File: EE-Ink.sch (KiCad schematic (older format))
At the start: 32 parts

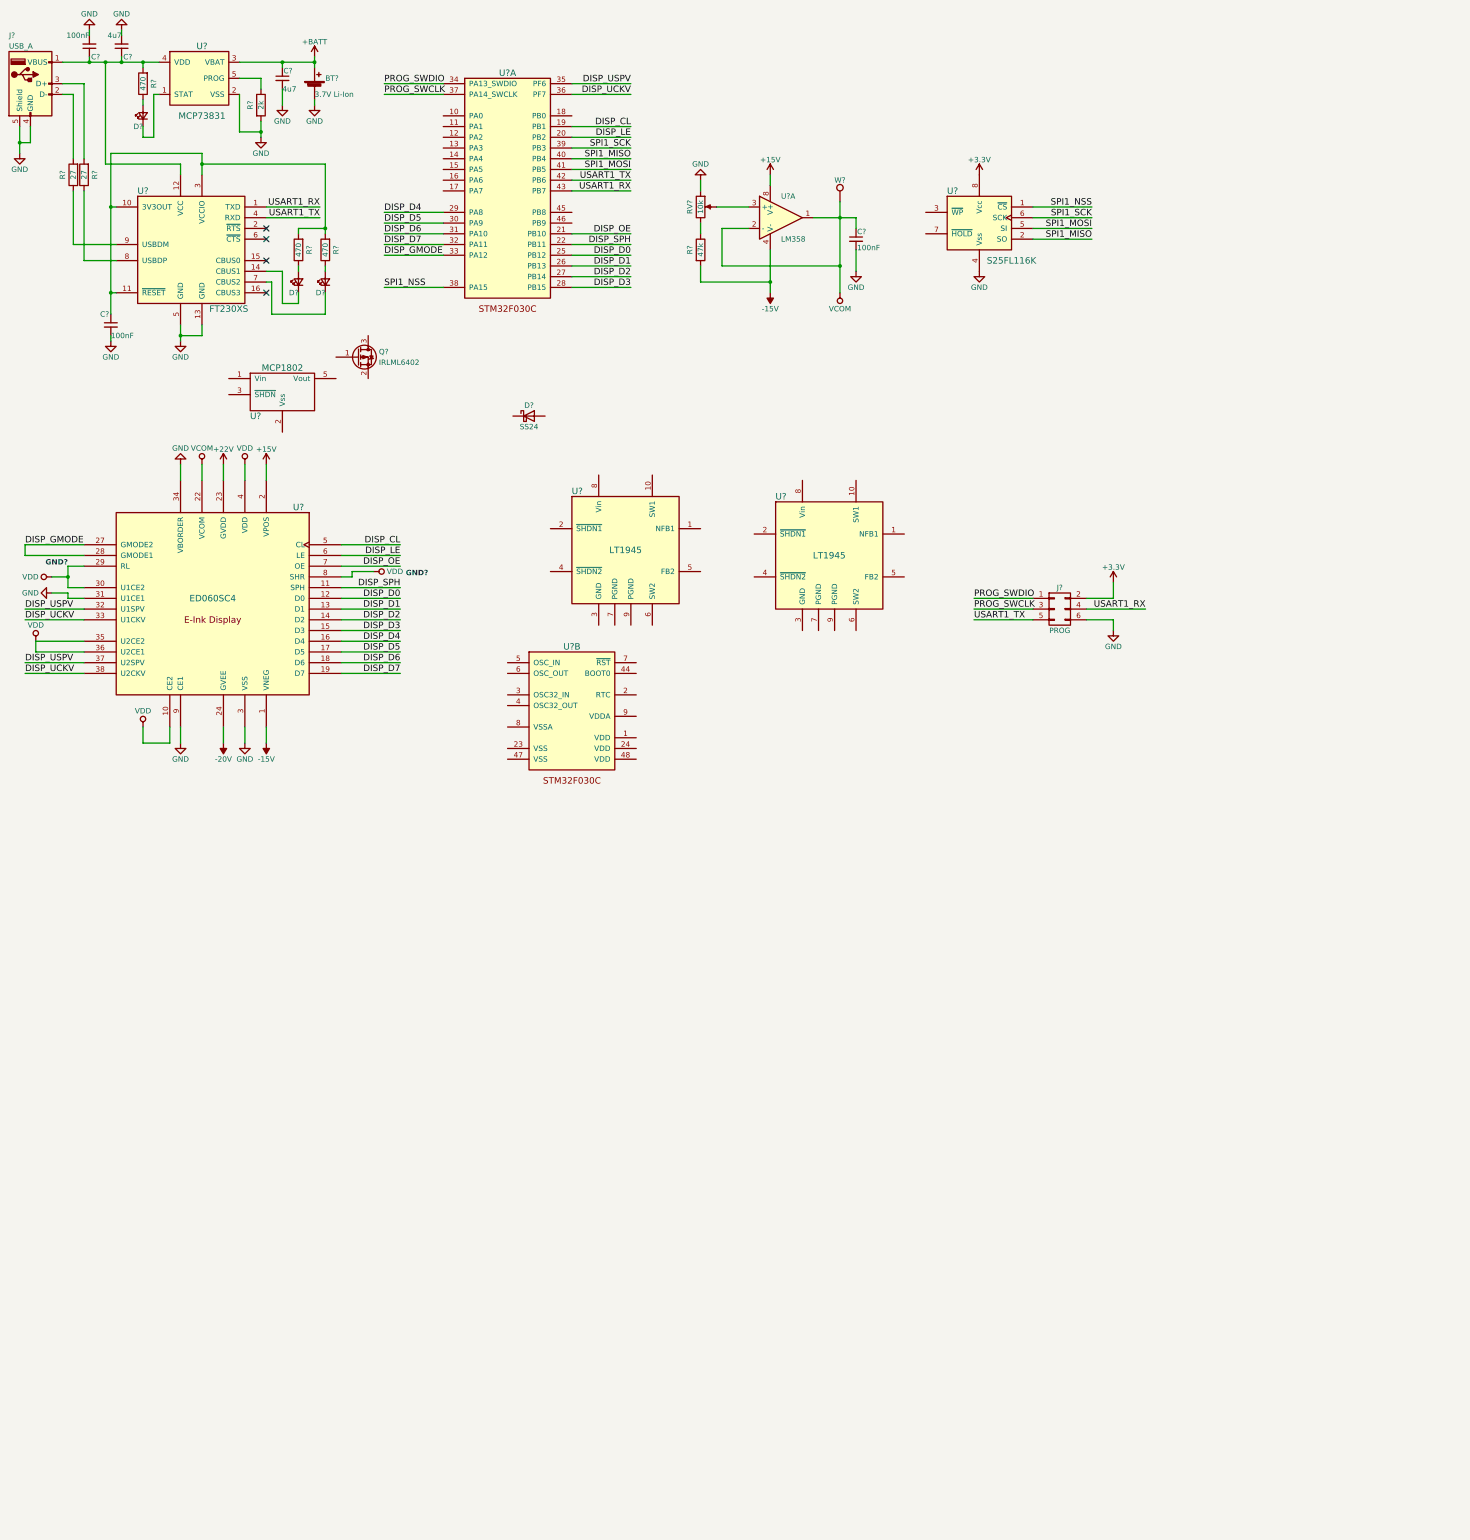
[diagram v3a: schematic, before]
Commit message: Wired up first boost circuit according to example.
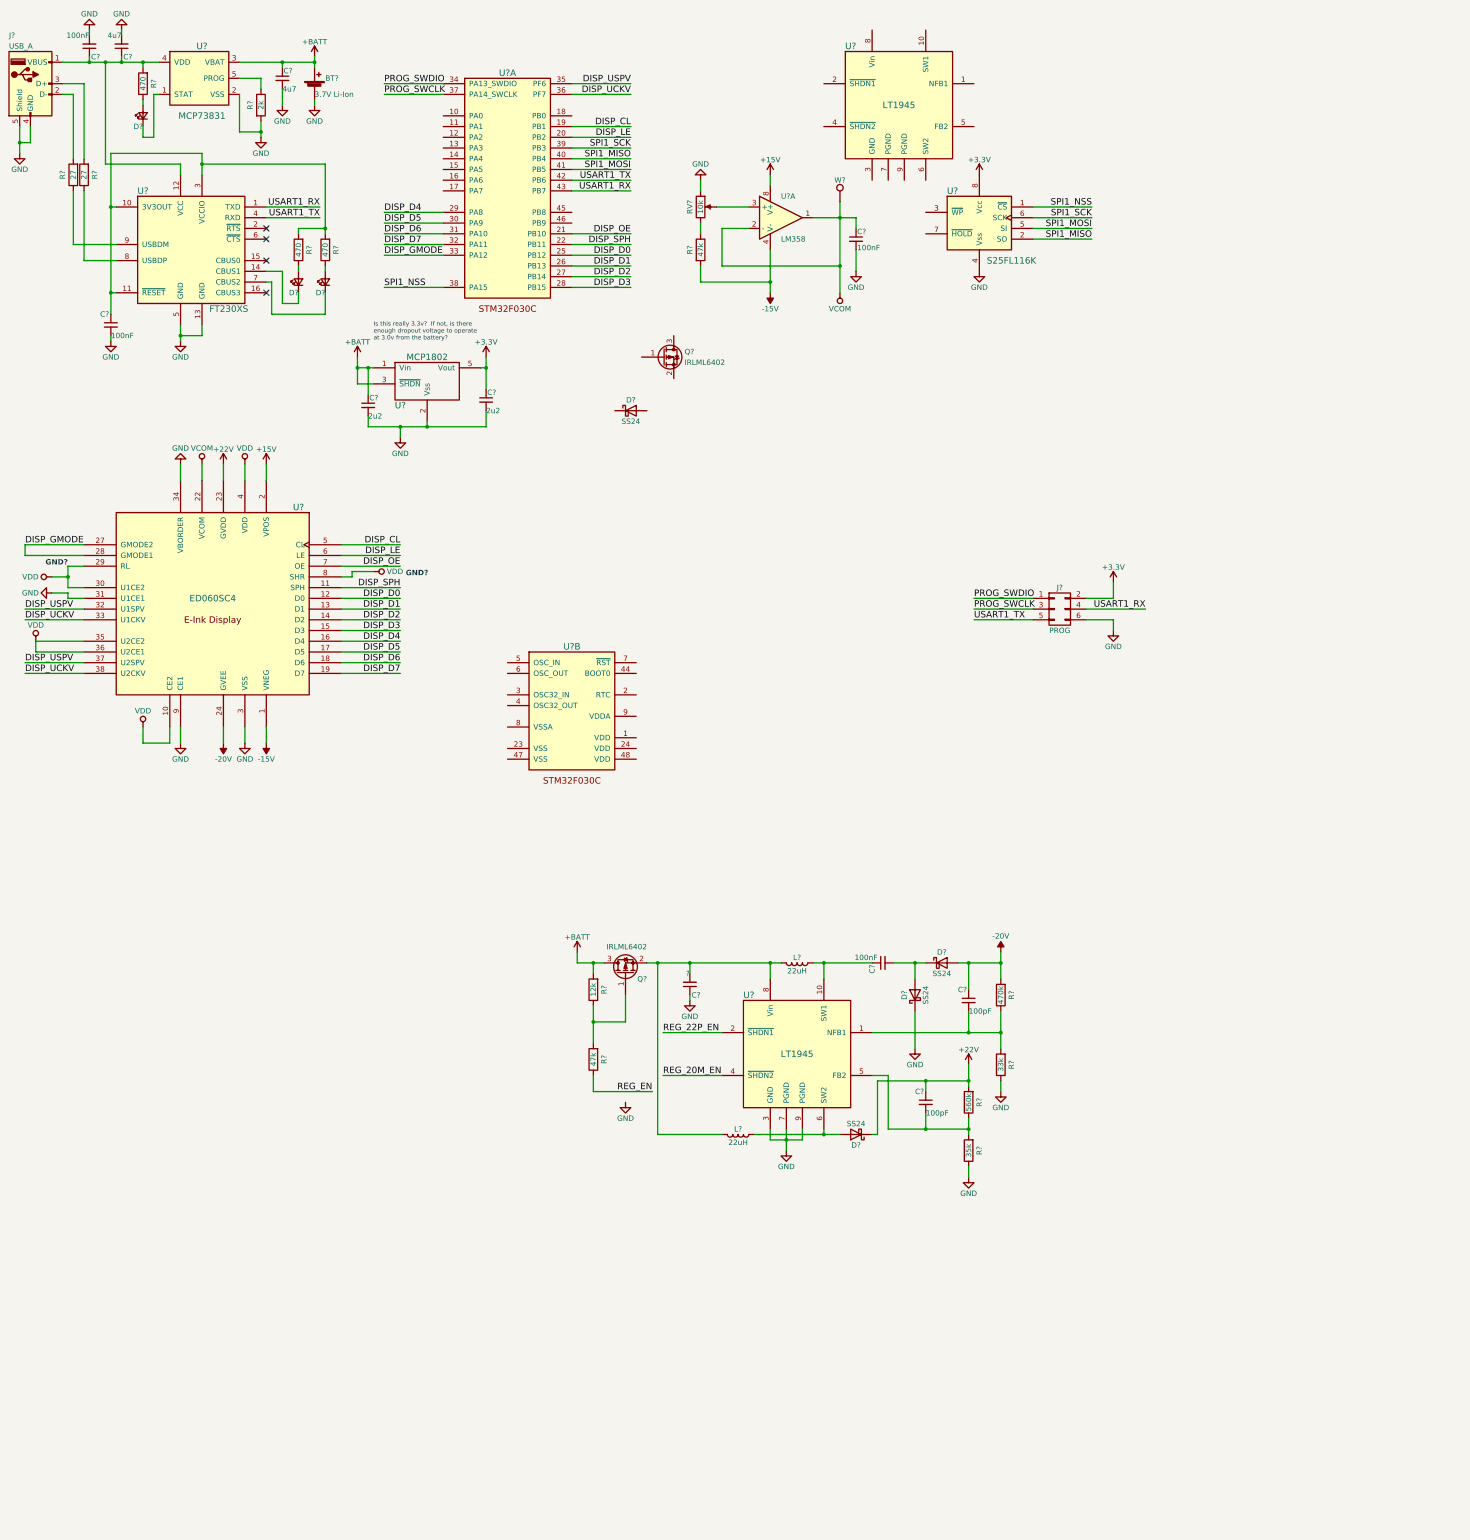
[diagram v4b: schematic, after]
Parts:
- added C? (x2): 2u2, symbol C_Small
- added C?: ?, symbol C_Small
- added C?: 100nF, symbol C_Small
- added C? (x2): 100pF, symbol C_Small
- added D? (x3): SS24, symbol D_Schottky
- added L? (x2): 22uH, symbol L
- added Q?: IRLML6402, symbol Q_PMOS_GSD
- added R?: 12k, symbol R
- added R?: 47k, symbol R
- added R?: 470k, symbol R
- added R?: 33k, symbol R
- added R?: 560k, symbol R
- added R?: 35k, symbol R
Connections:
- net +22V: now also C?.1, D?.1 (K), R?.2
- net +3V3: now also U?.5 (Vout), C?.1
- net +BATT: now also U?.1 (Vin), U?.3 (~SHDN), C?.1, Q?.3 (D), R?.2
- net -20V: now also C?.1, D?.2 (A), R?.2
- net GND: now also U?.2 (Vss), U?.3 (GND), U?.7 (PGND), U?.9 (PGND), C?.1, C?.2, C?.2, D?.1 (K), R?.1, R?.1
- net at U?.1 (NFB1): now also C?.2, R?.1, R?.2
- net at U?.10 (SW1): now also C?.1, L?.1
- net REG_22P_EN: now reaches U?.2 (~SHDN1)
- net REG_20M_EN: now reaches U?.4 (~SHDN2)
- net at U?.5 (FB2): now also C?.2, R?.1, R?.2
- net at U?.6 (SW2): now also D?.2 (A), L?.1
- net at U?.8 (Vin): now also C?.2, L?.2, L?.2, Q?.2 (S)
- new net: Q?.1 (G), R?.1, R?.2
- new net: C?.2, D?.1 (K), D?.2 (A)
- new net REG_EN: R?.1
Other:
- note added: "Is this really 3.3v? If not, is there \nenough dropout voltage to operate \nat 3.0v from the battery?"
- moved on the sheet: D?, Q?, U?

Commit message: Minor changes.
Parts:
- C?: value ? -> 4u7
- C?: value 100pF -> 4p7
- R?: value 35k -> 33k
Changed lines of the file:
@@
 Text Notes 3950 3600 0    40   ~ 0
 Is this really 3.3v?  If not, is there \nenough dropout voltage to operate \nat 3.0v from the battery?
-$Comp
-L GND #PWR?
-U 1 1 58DF7B78
-P 6300 10700
-F 0 "#PWR?" H 6300 10450 50  0001 C CNN
-F 1 "GND" H 6300 10550 50  0000 C CNN
-F 2 "" H 6300 10700 50  0001 C CNN
-F 3 "" H 6300 10700 50  0001 C CNN
-	1    6300 10700
-	1    0    0    -1
-$EndComp
 Text Label 6650 10050 0    60   ~ 0
 REG_22P_EN
@@
 P 6900 9600
 F 0 "C?" H 6800 9700 50  0000 L CNN
-F 1 "?" H 6900 9500 50  0000 L CNN
+F 1 "4u7" H 6950 9550 50  0000 L CNN
 F 2 "" H 6900 9600 50  0001 C CNN
 F 3 "" H 6900 9600 50  0001 C CNN
@@
 P 9100 10700
 F 0 "C?" H 9000 10800 50  0000 L CNN
-F 1 "100pF" H 9100 10600 50  0000 L CNN
+F 1 "4p7" H 9100 10600 50  0000 L CNN
 F 2 "" H 9100 10700 50  0001 C CNN
 F 3 "" H 9100 10700 50  0001 C CNN
@@
 P 9500 11150
 F 0 "R?" V 9400 11150 50  0000 C CNN
-F 1 "35k" V 9500 11150 50  0000 C CNN
+F 1 "33k" V 9500 11150 50  0000 C CNN
 F 2 "" V 9430 11150 50  0001 C CNN
 F 3 "" H 9500 11150 50  0001 C CNN

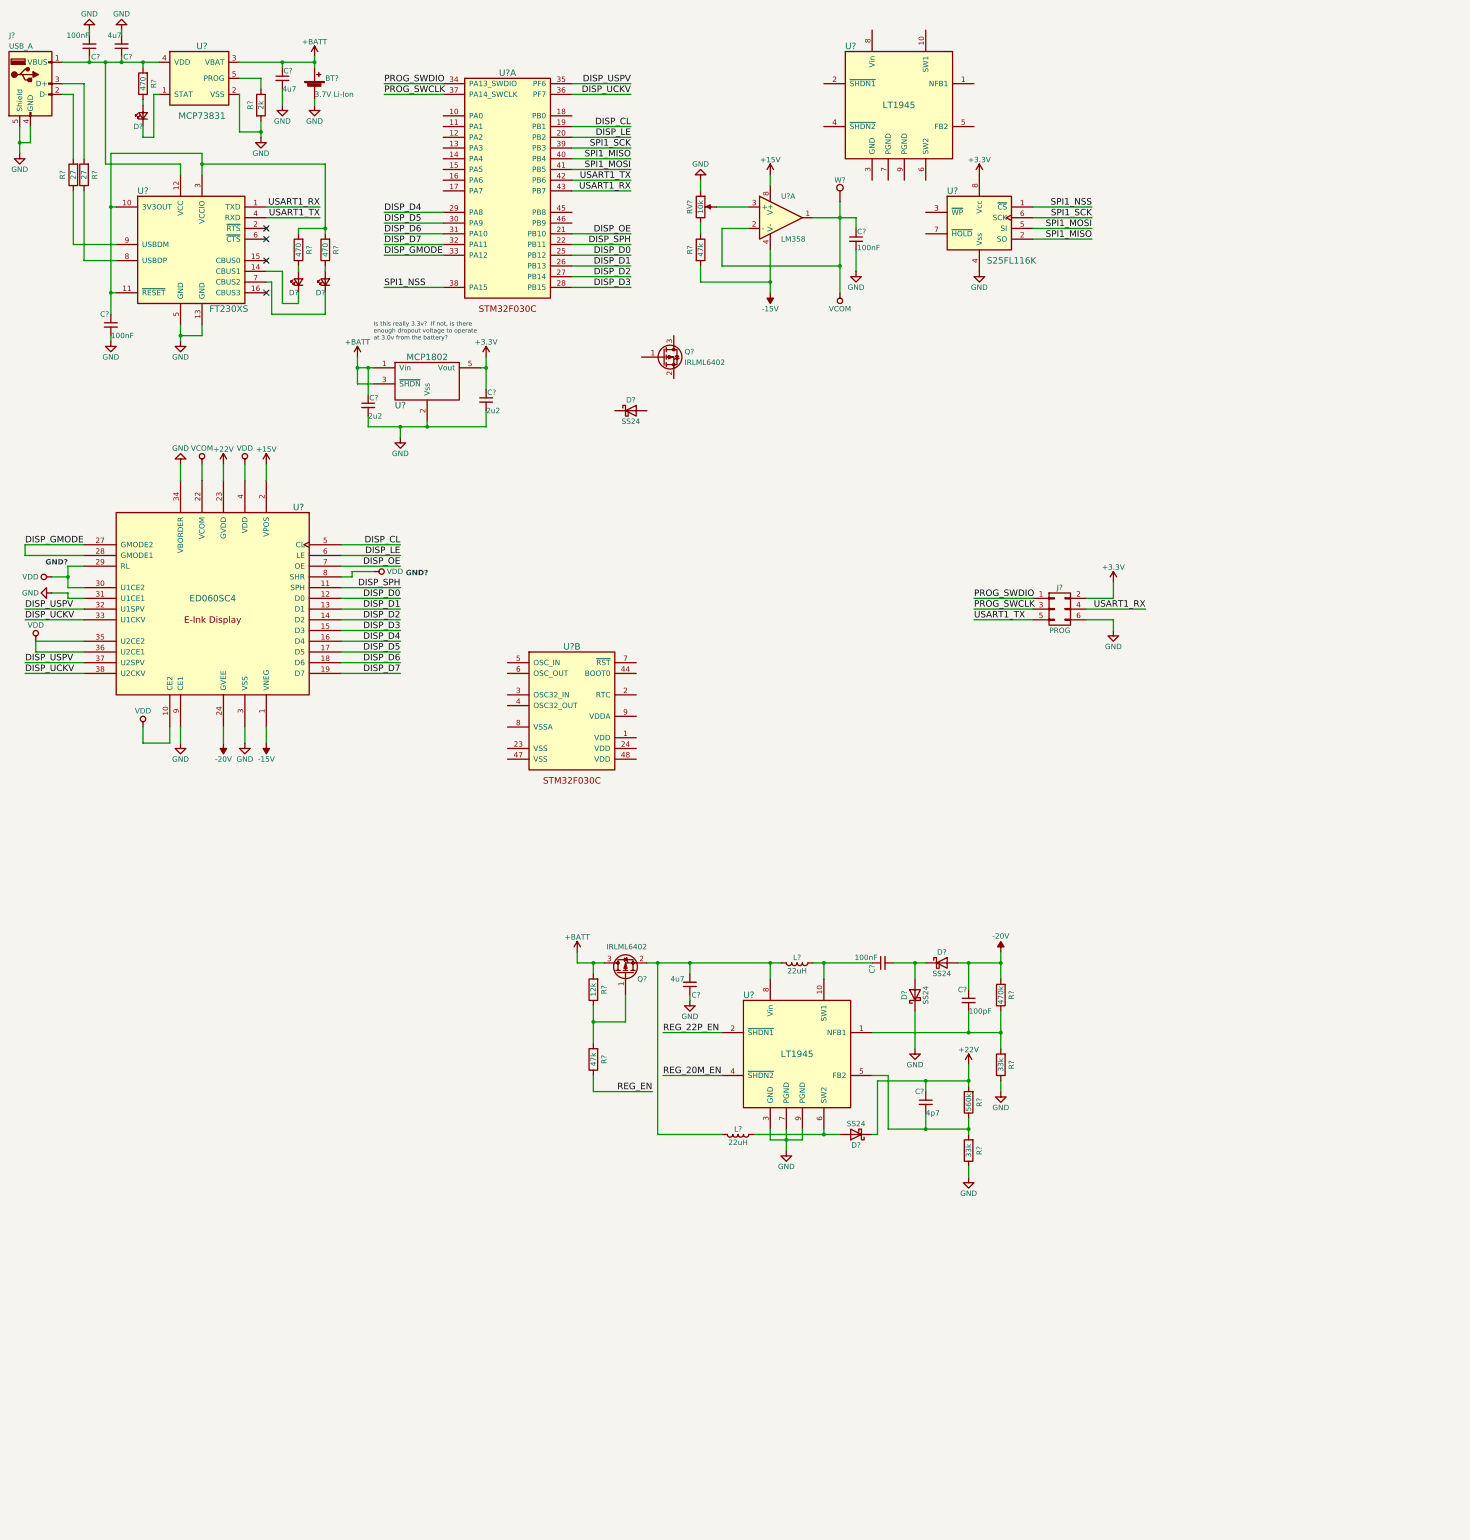
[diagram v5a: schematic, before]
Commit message: Wired up second dc-dc converter and connected related I/O to mcu.
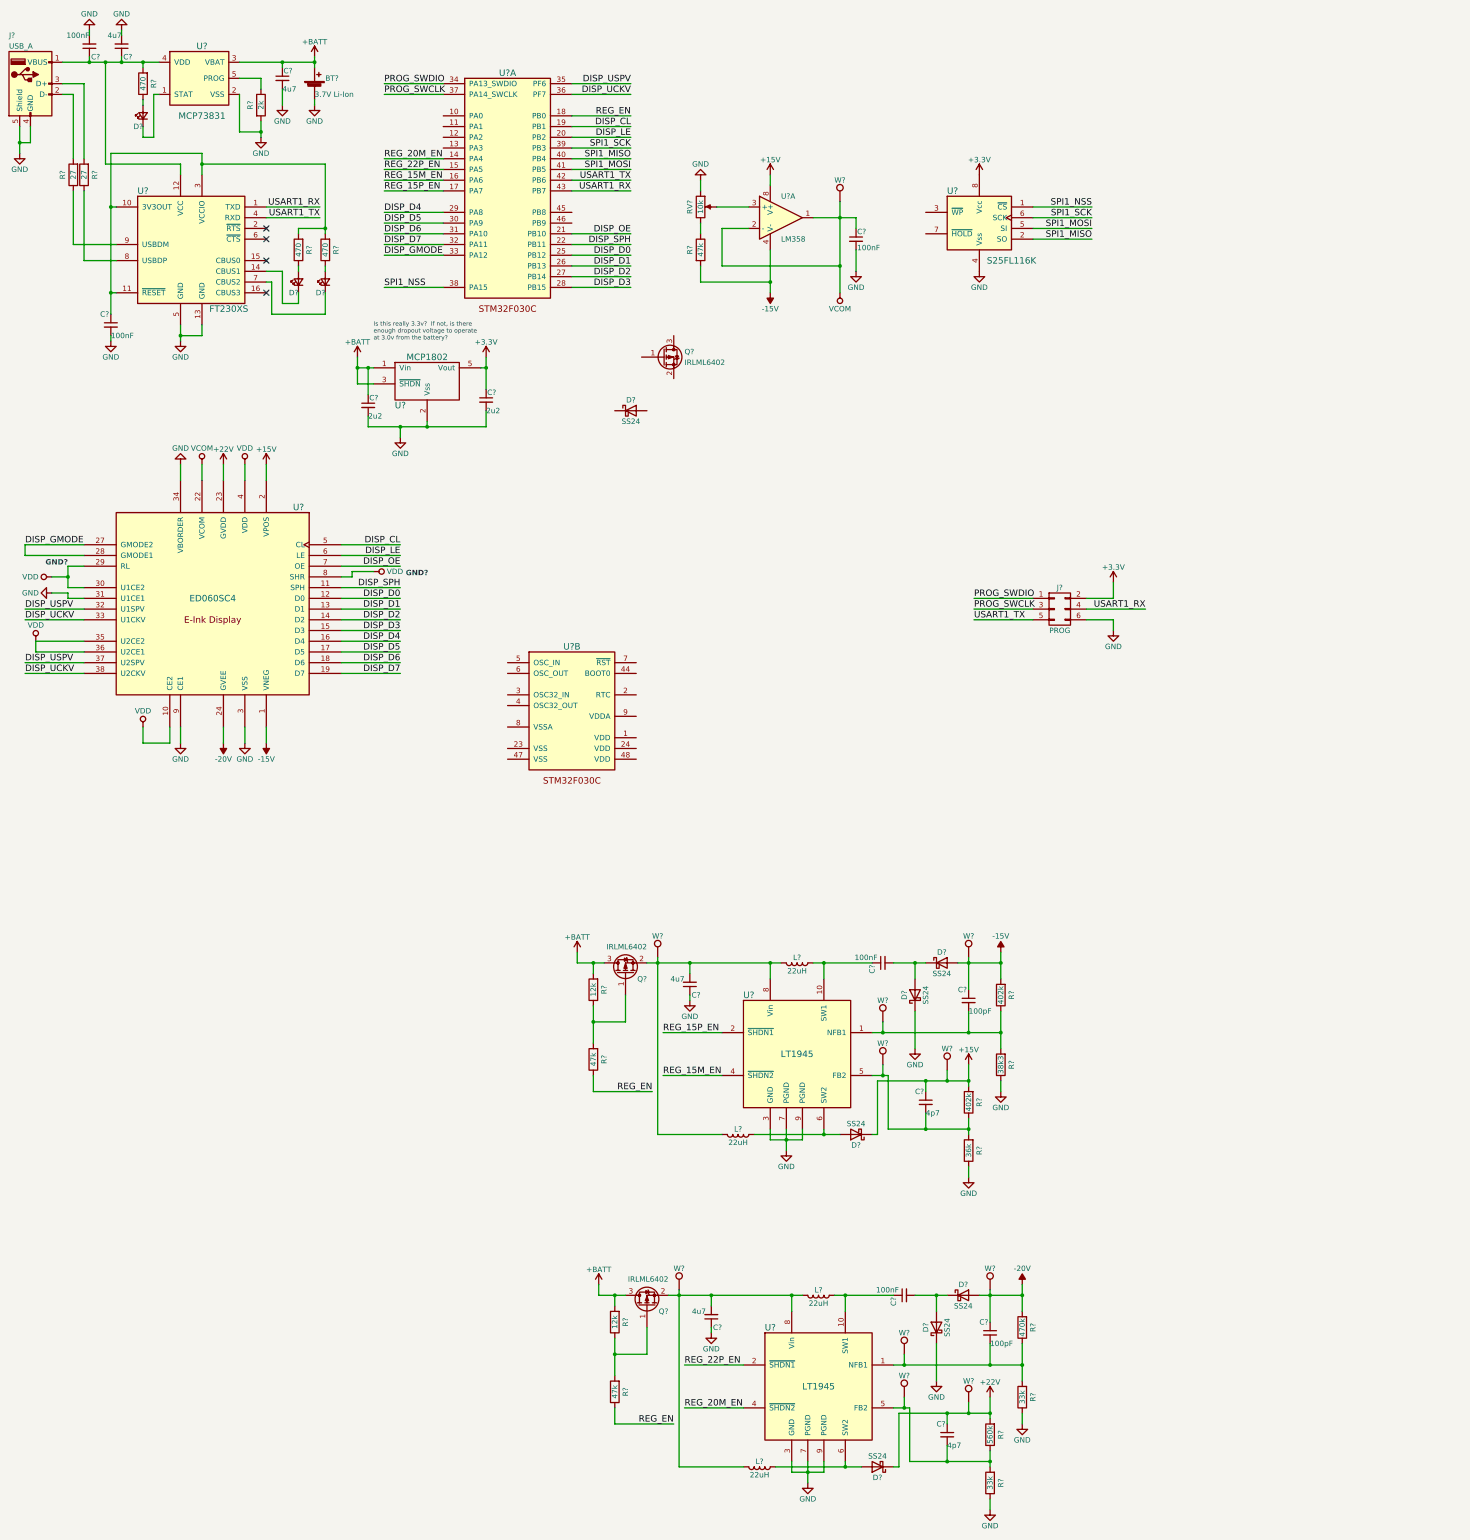
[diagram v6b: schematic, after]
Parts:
- removed U?: LT1945, symbol LT1945
- added C?: 4u7, symbol C_Small
- added C?: 100nF, symbol C_Small
- added C?: 100pF, symbol C_Small
- added C?: 4p7, symbol C_Small
- added D? (x3): SS24, symbol D_Schottky
- added L? (x2): 22uH, symbol L
- added Q?: IRLML6402, symbol Q_PMOS_GSD
- added R?: 12k, symbol R
- added R?: 47k, symbol R
- added R?: 470k, symbol R
- added R? (x2): 33k, symbol R
- added R?: 560k, symbol R
- added U?: LT1945, symbol LT1945
- added W? (x10): TEST_1P, symbol TEST_1P
- R?: value 470k -> 402k
- R?: value 33k -> 38k3
- R?: value 560k -> 402k
- R?: value 33k -> 36k
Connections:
- net +15V: now also C?.1, D?.1 (K), R?.2, W?.1
- net +22V: now also C?.1, D?.1 (K), R?.2, W?.1; no longer C?.1, D?.1 (K), R?.2
- net +BATT: now also Q?.3 (D), R?.2
- net -15V: now also C?.1, D?.2 (A), R?.2, W?.1
- net -20V: now also C?.1, D?.2 (A), R?.2, W?.1; no longer C?.1, D?.2 (A), R?.2
- net GND: now also C?.1, D?.1 (K), R?.1, R?.1, U?.3 (GND), U?.7 (PGND), U?.9 (PGND)
- net REG_20M_EN: now also U?.14 (PA4), U?.4 (~SHDN2); no longer U?.4 (~SHDN2)
- net REG_22P_EN: now also U?.15 (PA5), U?.2 (~SHDN1); no longer U?.2 (~SHDN1)
- net REG_EN: now also U?.18 (PB0), R?.1
- net REG_15M_EN: now reaches U?.16 (PA6)
- net REG_15M_EN: now also U?.4 (~SHDN2)
- net REG_15P_EN: now reaches U?.17 (PA7)
- net REG_15P_EN: now also U?.2 (~SHDN1)
- net at C?.2, R?.1, R?.2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: now also W?.1 (x2)
- net at C?.2, L?.2, L?.2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: now also W?.1
- new net: C?.2, R?.1, R?.2, U?.1 (NFB1), W?.1
- new net: C?.1, L?.1, U?.10 (SW1)
- new net: C?.2, R?.1, R?.2, U?.5 (FB2), W?.1
- new net: D?.2 (A), L?.1, U?.6 (SW2)
- new net: C?.2, L?.2, L?.2, Q?.2 (S), U?.8 (Vin), W?.1
- new net: Q?.1 (G), R?.1, R?.2
- new net: C?.2, D?.1 (K), D?.2 (A)
